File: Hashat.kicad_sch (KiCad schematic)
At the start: 1 part, among them J1 Raspberry_Pi_2_3

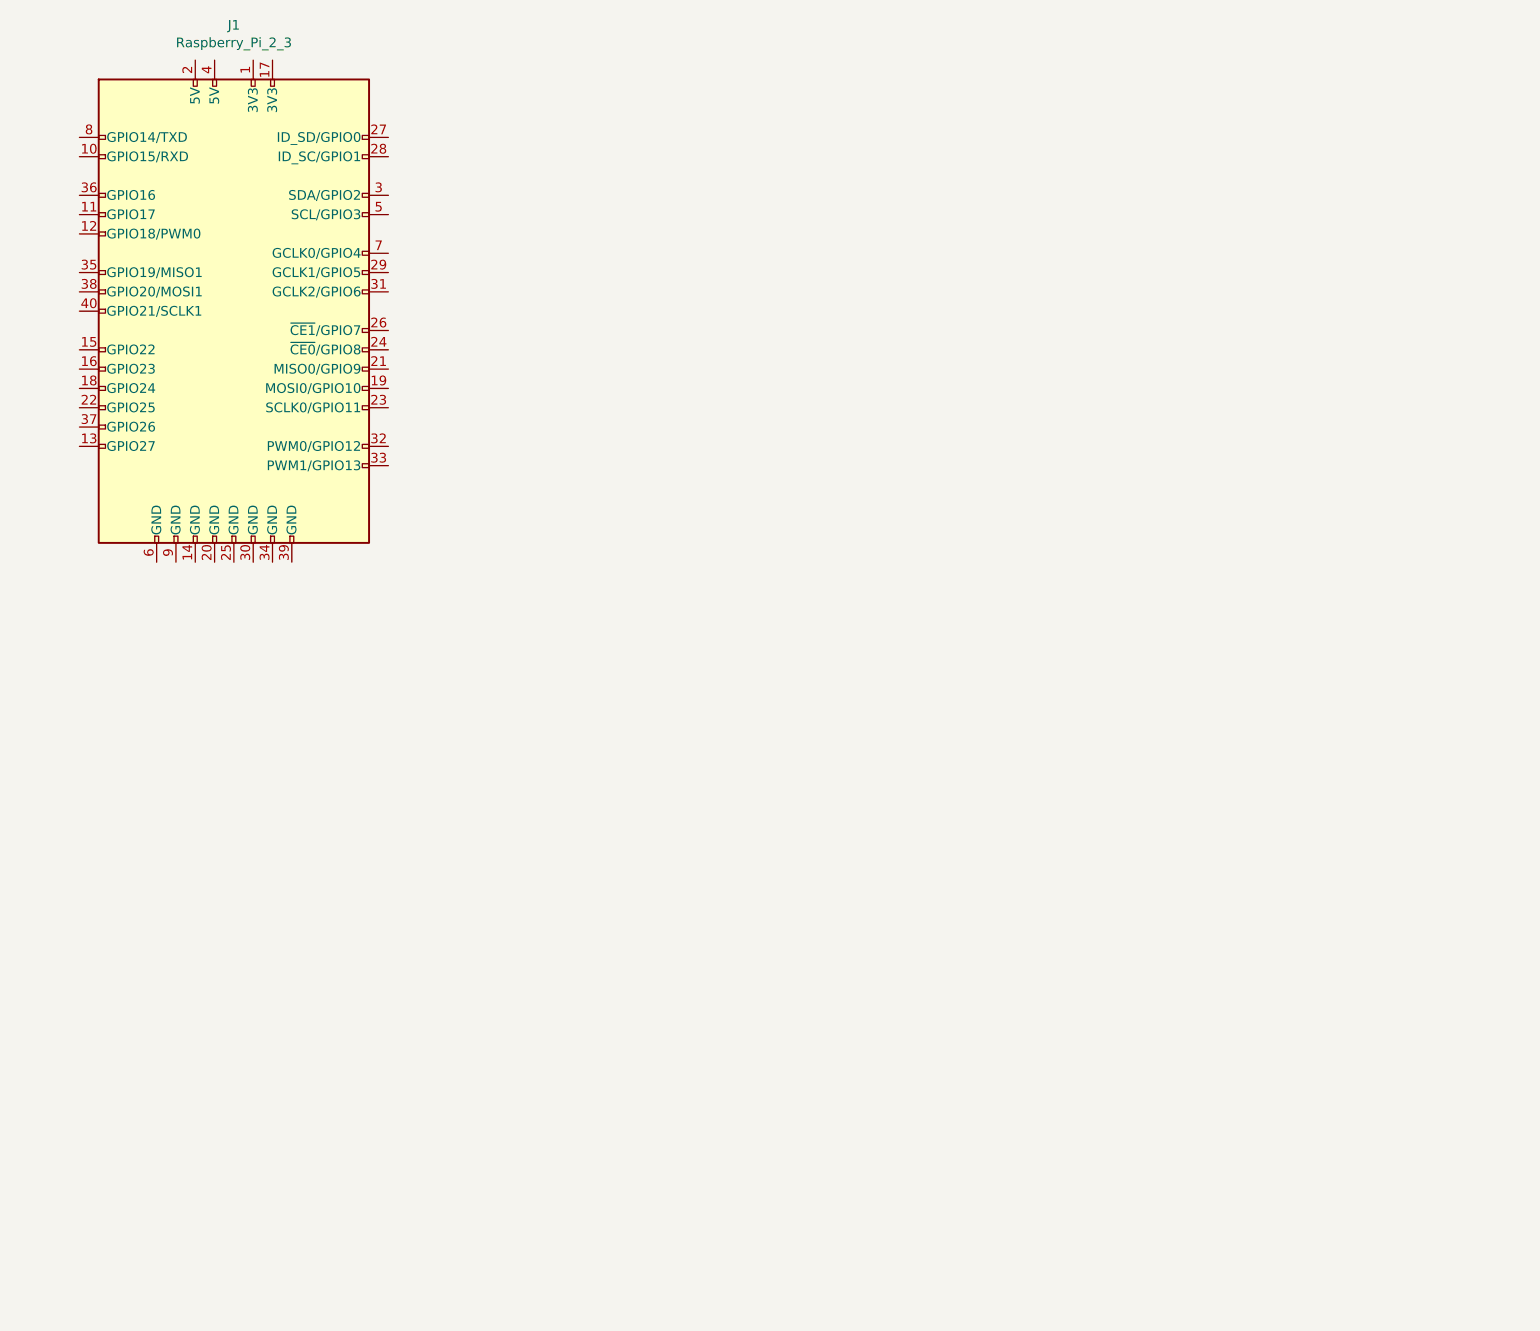
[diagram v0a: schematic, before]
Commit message: Added some placeholder sheets
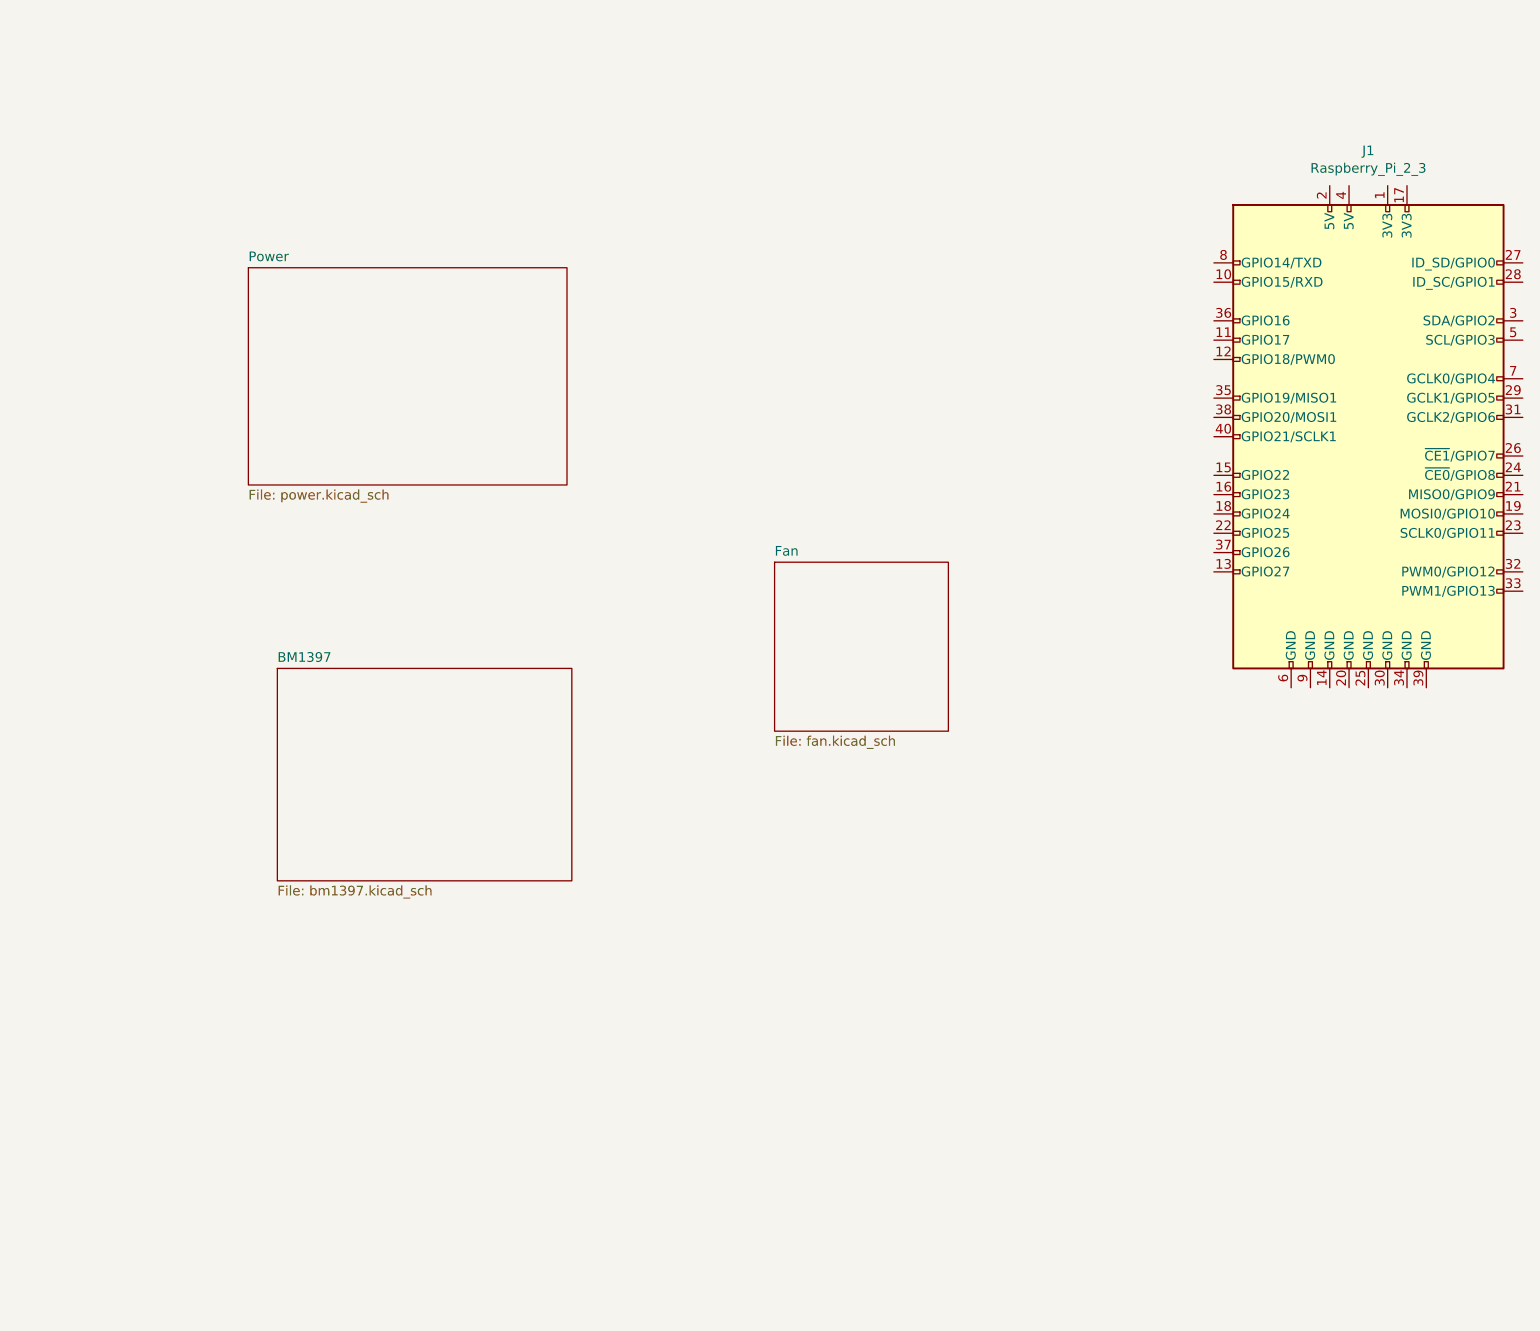
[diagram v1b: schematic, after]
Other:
- added sheet BM1397 (bm1397.kicad_sch)
- added sheet Fan (fan.kicad_sch)
- added sheet Power (power.kicad_sch)
- moved on the sheet: J1
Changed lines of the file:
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@@
     (date "2023-04-21")
   )
-  (symbol (lib_id "Connector:Raspberry_Pi_2_3") (at 52.07 50.8 0) (unit 1)
+  (symbol (lib_id "Connector:Raspberry_Pi_2_3") (at 201.295 67.31 0) (unit 1)
     (in_bom yes) (on_board yes) (dnp no)
-    (property "Reference" "J1" (at 52.07 13.1826 0)
+    (property "Reference" "J1" (at 201.295 29.6926 0)
       (effects (font (size 1.27 1.27)))
     )
-    (property "Value" "Raspberry_Pi_2_3" (at 52.07 15.494 0)
+    (property "Value" "Raspberry_Pi_2_3" (at 201.295 32.004 0)
       (effects (font (size 1.27 1.27)))
     )
-    (property "Footprint" "pihat:ESQ-120-14-T-D" (at 52.07 50.8 0)
+    (property "Footprint" "pihat:ESQ-120-14-T-D" (at 201.295 67.31 0)
       (effects (font (size 1.27 1.27)) hide)
     )
-    (property "Datasheet" "https://www.raspberrypi.org/documentation/hardware/raspberrypi/schematics/rpi_SCH_3bplus_1p0_reduced.pdf" (at 52.07 50.8 0)
+    (property "Datasheet" "https://www.raspberrypi.org/documentation/hardware/raspberrypi/schematics/rpi_SCH_3bplus_1p0_reduced.pdf" (at 201.295 67.31 0)
       (effects (font (size 1.27 1.27)) hide)
     )
@@
       )
     )
+  )
+  (sheet (at 57.785 97.79) (size 38.735 27.94) (fields_autoplaced)
+    (stroke (width 0.1524) (type solid))
+    (fill (color 255 255 194 1.0000))
+    (property "Sheetname" "BM1397" (at 57.785 97.0784 0)
+      (effects (font (size 1.27 1.27)) (justify left bottom))
+    )
+    (property "Sheetfile" "bm1397.kicad_sch" (at 57.785 126.3146 0)
+      (effects (font (size 1.27 1.27)) (justify left top))
+    )
+    (instances
+      (project "Hashat"
+        (path "/00740941-7ad8-466a-a267-188591e2b5c4" (page "2"))
+      )
+    )
+  )
+  (sheet (at 53.975 45.085) (size 41.91 28.575) (fields_autoplaced)
+    (stroke (width 0.1524) (type solid))
+    (fill (color 255 255 194 1.0000))
+    (property "Sheetname" "Power" (at 53.975 44.3734 0)
+      (effects (font (size 1.27 1.27)) (justify left bottom))
+    )
+    (property "Sheetfile" "power.kicad_sch" (at 53.975 74.2446 0)
+      (effects (font (size 1.27 1.27)) (justify left top))
+    )
+    (instances
+      (project "Hashat"
+        (path "/00740941-7ad8-466a-a267-188591e2b5c4" (page "3"))
+      )
+    )
+  )
+  (sheet (at 123.19 83.82) (size 22.86 22.225) (fields_autoplaced)
+    (stroke (width 0.1524) (type solid))
+    (fill (color 255 255 194 1.0000))
+    (property "Sheetname" "Fan" (at 123.19 83.1084 0)
+      (effects (font (size 1.27 1.27)) (justify left bottom))
+    )
+    (property "Sheetfile" "fan.kicad_sch" (at 123.19 106.6296 0)
+      (effects (font (size 1.27 1.27)) (justify left top))
+    )
+    (instances
+      (project "Hashat"
+        (path "/00740941-7ad8-466a-a267-188591e2b5c4" (page "4"))
+      )
+    )
